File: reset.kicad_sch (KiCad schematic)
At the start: 46 parts, among them J7 BM08B-SRSS-TB-LF-SN, Q8 DTC014TEBTL, Q9 DTC014TEBTL, U31 TPS3840PH30DBVR, U32 TPS3840PH30DBVR, U33 74AVC4T245RSVRG4, U34 SN74AVC2T245RSWR, U35 SN74LVC1G125DBVR, U36 74LCX07BQX

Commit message: Added cosmetic changes to schematics (e.g. position of labels, designators)
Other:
- moved on the sheet: C130, C132, C134, C136, C137, C138, D4, J7, TP17, TP18, TP19, TP20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

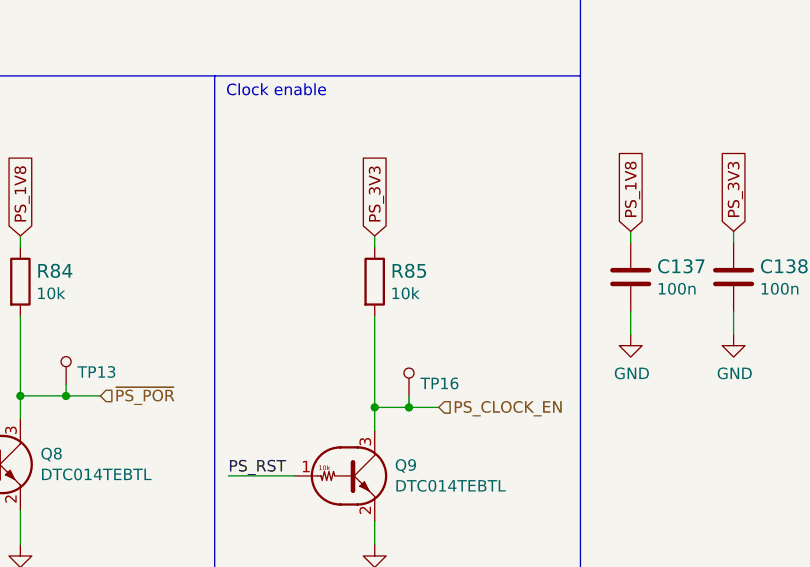
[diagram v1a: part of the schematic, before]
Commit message: Added missing capacitors to ethernet jack
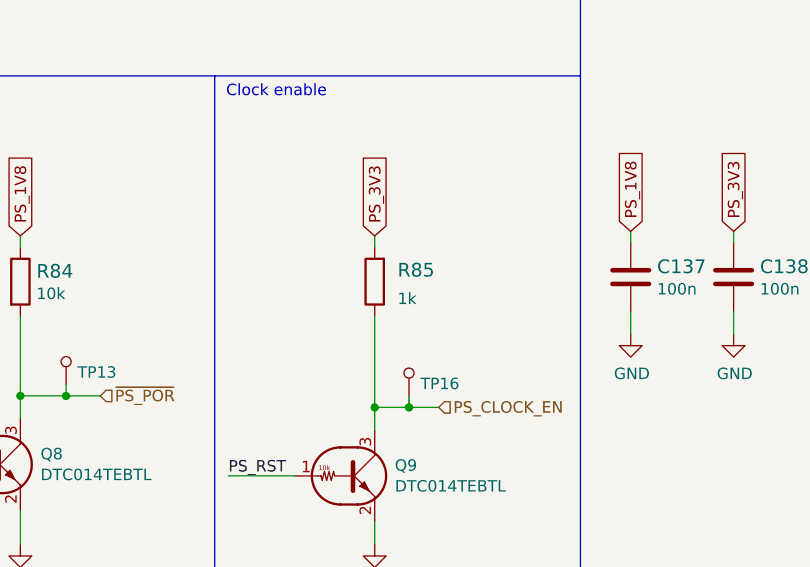
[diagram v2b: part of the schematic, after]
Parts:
- removed R85: R_10k_0402, kria-k26-devboard-footprints:0402-res, symbol kria-k26-devboard:R_10k_0402
- added R85: R_1k_0402, antmicro-footprints:0402-res, symbol antmicroResistors0402:R_1k_0402
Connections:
- net PS_3V3: now also R85.2
- net PS_CLOCK_EN: now also R85.1
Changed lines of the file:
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@@
     (pin "1")
-  )
-  (symbol (lib_id "kria-k26-devboard:R_10k_0402") (at 111.76 130.81 270) (unit 1)
-    (in_bom yes) (on_board yes)
-    (property "Reference" "R85" (id 0) (at 113.538 129.667 90)
-      (effects (font (size 1.524 1.524)) (justify left))
-    )
-    (property "Value" "R_10k_0402" (id 1) (at 107.95 130.81 0)
-      (effects (font (size 1.524 1.524)) hide)
-    )
-    (property "Footprint" "kria-k26-devboard-footprints:0402-res" (id 2) (at 116.84 135.89 0)
-      (effects (font (size 1.524 1.524)) (justify left) hide)
-    )
-    (property "Datasheet" "" (id 3) (at 111.76 130.81 0)
-      (effects (font (size 1.27 1.27)) hide)
-    )
-    (property "Manufacturer" "VISHAY" (id 4) (at 121.92 135.89 0)
-      (effects (font (size 1.524 1.524)) (justify left) hide)
-    )
-    (property "MPN" "CRCW040210K0FKEDHP" (id 5) (at 119.38 135.89 0)
-      (effects (font (size 1.524 1.524)) (justify left) hide)
-    )
-    (property "Val" "10k" (id 6) (at 113.538 132.1562 90)
-      (effects (font (size 1.27 1.27)) (justify left))
-    )
-    (pin "1")
-    (pin "2")
   )
   (symbol (lib_id "kria-k26-devboard:R_10k_0402") (at 72.39 130.81 270) (unit 1)
@@
     (pin "1")
   )
+  (symbol (lib_id "antmicroResistors0402:R_1k_0402") (at 111.76 130.81 90) (unit 1)
+    (in_bom yes) (on_board yes) (fields_autoplaced)
+    (property "Reference" "R85" (id 0) (at 114.3 129.54 90)
+      (effects (font (size 1.524 1.524)) (justify right))
+    )
+    (property "Value" "R_1k_0402" (id 1) (at 115.57 130.81 0)
+      (effects (font (size 1.524 1.524)) hide)
+    )
+    (property "Footprint" "antmicro-footprints:0402-res" (id 2) (at 106.68 125.73 0)
+      (effects (font (size 1.524 1.524)) (justify left) hide)
+    )
+    (property "Datasheet" "" (id 3) (at 111.76 130.81 0)
+      (effects (font (size 1.27 1.27)) hide)
+    )
+    (property "Manufacturer" "BOURNS" (id 4) (at 101.6 125.73 0)
+      (effects (font (size 1.524 1.524)) (justify left) hide)
+    )
+    (property "MPN" "CR0402-FX-1001GLF" (id 5) (at 104.14 125.73 0)
+      (effects (font (size 1.524 1.524)) (justify left) hide)
+    )
+    (property "Val" "1k" (id 6) (at 114.3 132.7149 90)
+      (effects (font (size 1.27 1.27)) (justify right))
+    )
+    (pin "1")
+    (pin "2")
+  )
 )

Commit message: loclib
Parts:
- R85: footprint antmicro-footprints:0402-res -> kria-k26-devboard-footprints:0402-res; symbol antmicroResistors0402:R_1k_0402 -> kria-k26-devboard:R_1k_0402

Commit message: Bump date and revision
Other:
- title: Reset logic -> Kria K26 Devboard
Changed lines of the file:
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@@
   (paper "A3")
   (title_block
-    (title "Reset logic")
-    (date "2022-07-25")
-    (rev "1.1.0")
+    (title "Kria K26 Devboard")
+    (date "2023-02-15")
+    (rev "1.1.1")
     (comment 1 "www.antmicro.com")
     (comment 2 "Antmicro Ltd.")

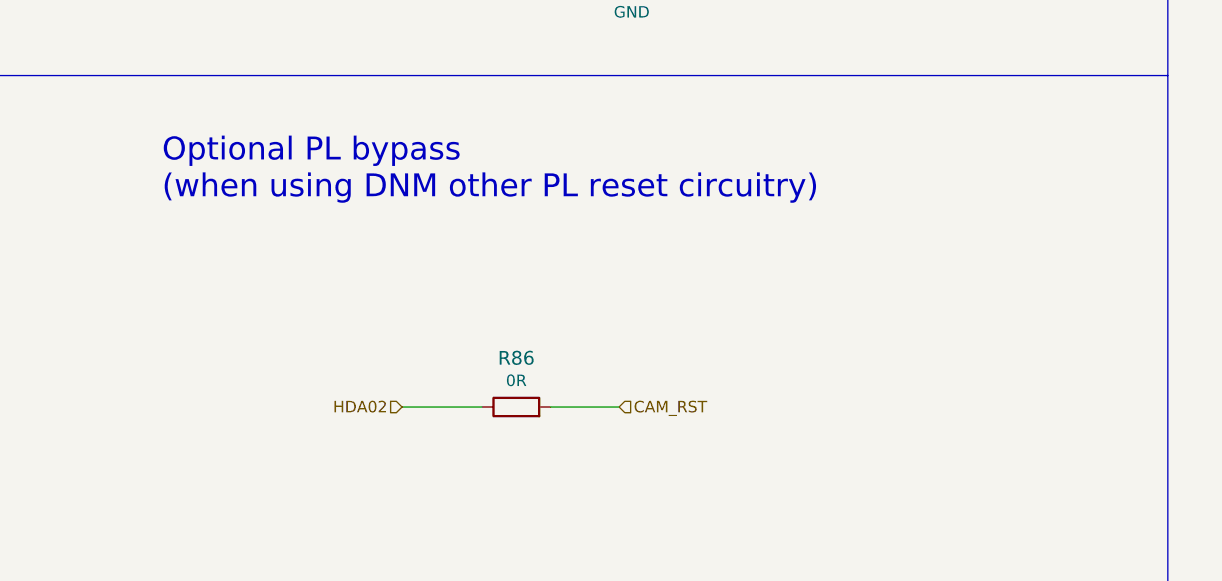
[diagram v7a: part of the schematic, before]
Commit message: Add decoupling to cammera and DP connector, schematic cleanup
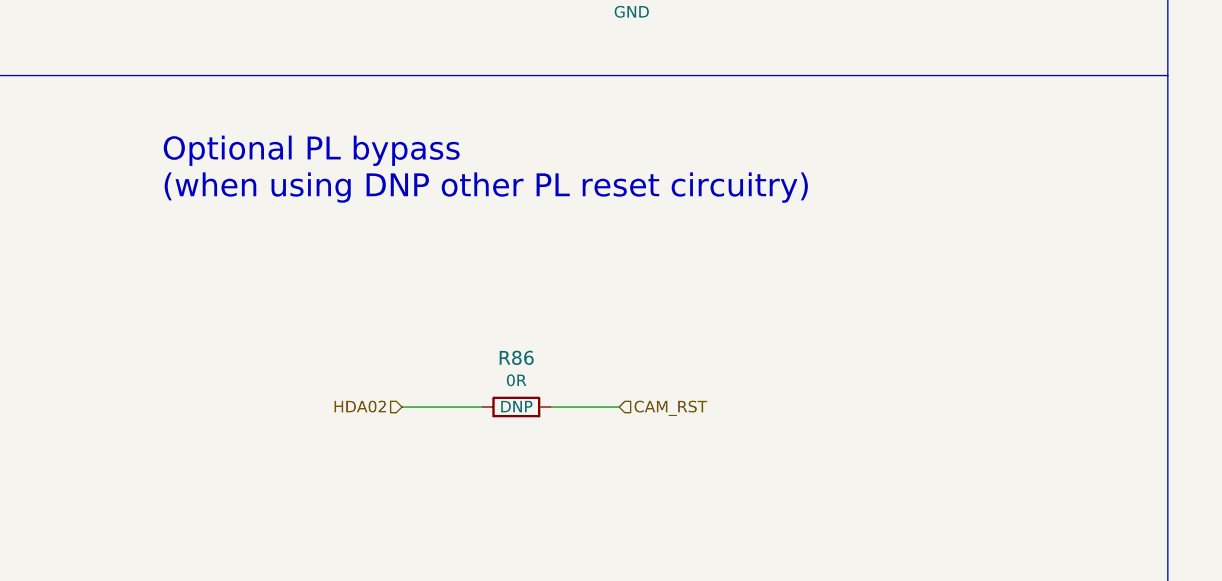
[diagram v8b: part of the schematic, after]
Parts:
- R86: DNP (none) -> DNP
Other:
- note added: "Optional PL bypass (when using DNP other PL reset circuitry)"
- note removed: "Optional PL bypass (when using DNM other PL reset circuitry)"
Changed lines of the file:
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@@
     (effects (font (size 1.27 1.27)) (justify left bottom))
   )
-  (text "Optional PL bypass \n(when using DNM other PL reset circuitry)"
+  (text "Optional PL bypass \n(when using DNP other PL reset circuitry)"
     (at 158.75 236.22 0)
     (effects (font (size 2.54 2.54)) (justify left bottom))
@@
     )
     (property "Val" "0R" (id 6) (at 198.12 256.159 0))
-    (pin "1")
-    (pin "2")
+    (property "DNP" "DNP" (id 7) (at 198.12 259.08 0))
+    (pin "1")
+    (pin "2")
